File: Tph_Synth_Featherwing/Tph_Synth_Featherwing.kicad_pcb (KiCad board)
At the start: 2 copper layers, 51 x 58.5 mm, 56 parts, among them J1 AudioJack3, J2 Conn_01x04, U1 PAM2401SCADJ, U2 LM2663M, U3 Opamp_Quad_Generic, U4 MCP4728

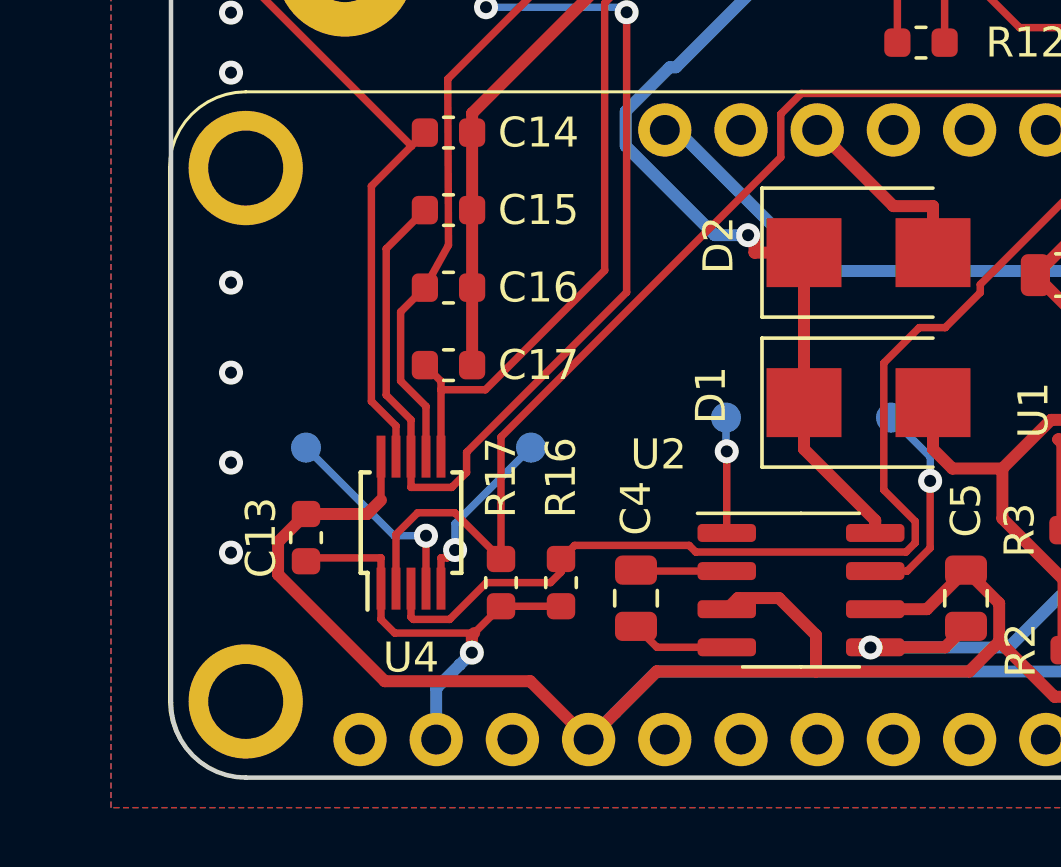
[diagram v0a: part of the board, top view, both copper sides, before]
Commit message: Add Qwiic connector to design
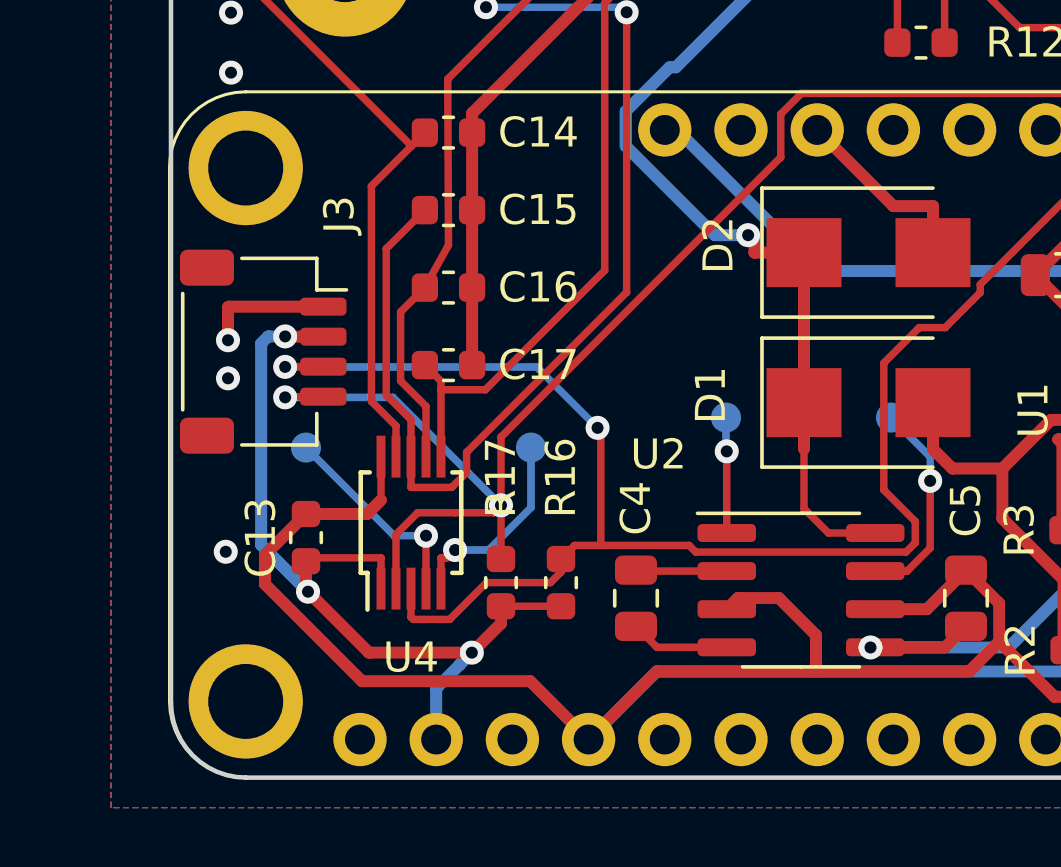
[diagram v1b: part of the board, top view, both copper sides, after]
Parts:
- added J3: Conn_01x04, Connector_JST:JST_SH_SM04B-SRSS-TB_1x04-1MP_P1.00mm_Horizontal, F.Cu at (90.1, 122.3)
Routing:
- net /F_SDA: track 49.7 -> 66.2 mm, vias 0 -> 2
- net +3V3: track 15.2 -> 29.3 mm, vias 1 -> 3
- net /F_SCL: track 48.8 -> 58.3 mm, vias 0 -> 2
- net GND: track 251.4 -> 256.5 mm, vias 33 -> 32
- net +5V: track 46.8 -> 47.8 mm
- net Net-(TP7-Pad1): track 6.06 -> 6.72 mm

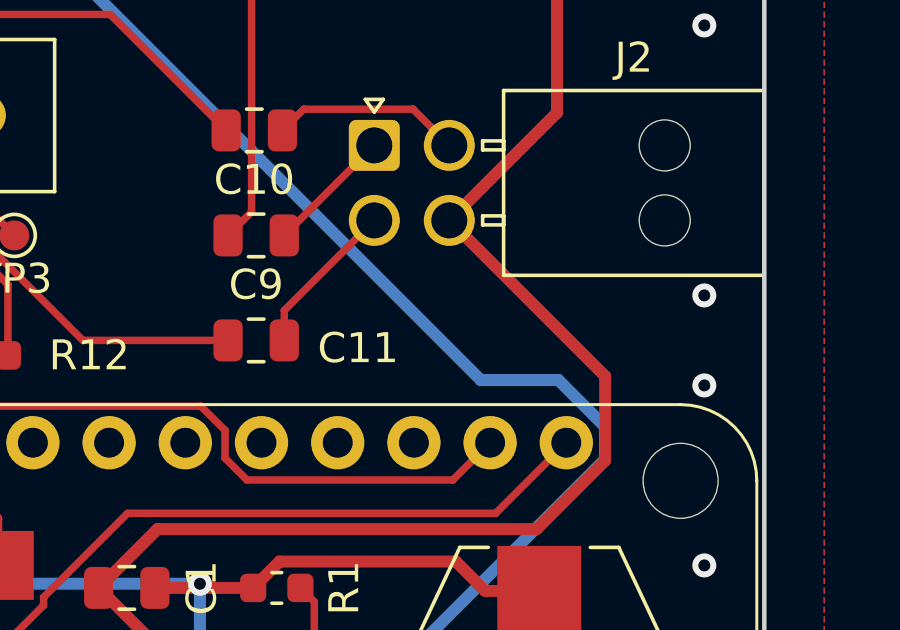
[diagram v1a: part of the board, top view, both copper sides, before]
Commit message: Improve/update silk screen
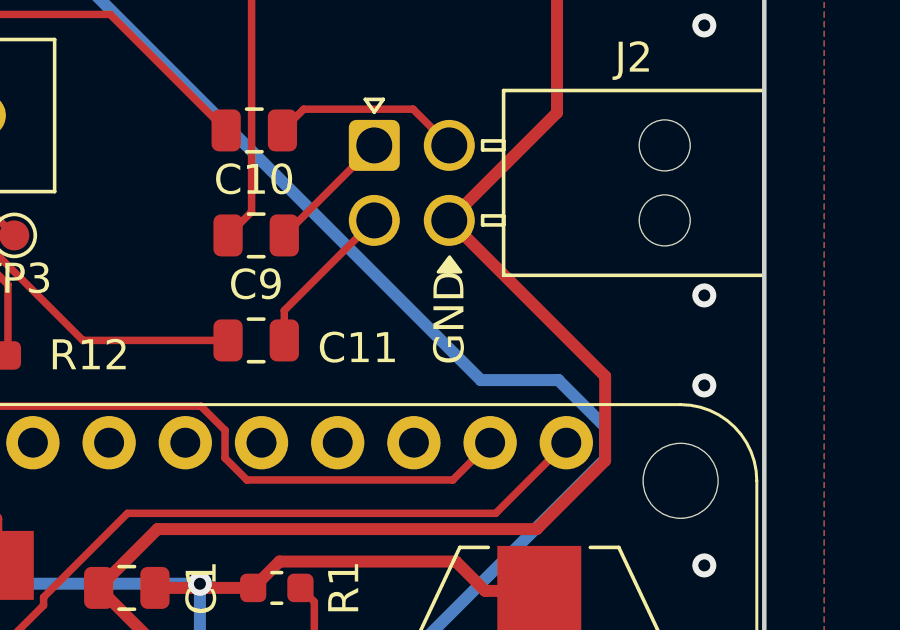
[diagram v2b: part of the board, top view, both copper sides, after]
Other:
- board text added: "3V3"
- board text added: "GND"
- board text added: "SCL"
- board text added: "SDA"
- board text added: "VBAT"
- board text added: "VUSB"
- board text added: "v0.3 20/12/2020 by Tisham (whatnick) Dhar OSHW TAPR"
- board text removed: "v0.2 01/02/2020 by Tisham (whatnick) Dhar OSHW TAPR"
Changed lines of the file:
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@@
       ))
   )
+  (gr_poly (pts
+ (xy 127.889 109.22)
+    (xy 127.127 109.22)
+    (xy 127.508 108.712)) (layer "F.SilkS") (width 0.1))
   (gr_arc (start 135.5 134) (end 135.5 136.5) (angle -90) (layer "Edge.Cuts") (width 0.15))
   (gr_arc (start 135.5 80.5) (end 138 80.5) (angle -90) (layer "Edge.Cuts") (width 0.15))
@@
   (gr_line (start 89.5 78) (end 135.5 78) (layer "Edge.Cuts") (width 0.15))
   (gr_line (start 135.5 136.5) (end 89.5 136.5) (layer "Edge.Cuts") (width 0.15))
+  (gr_text "GND" (at 100.838 132.588 270) (layer "B.SilkS")
+    (effects (font (size 1 1) (thickness 0.15)) (justify mirror))
+  )
+  (gr_text "SCL" (at 128.778 112.141 270) (layer "B.SilkS")
+    (effects (font (size 1 1) (thickness 0.15)) (justify mirror))
+  )
+  (gr_text "SDA" (at 131.445 112.141 270) (layer "B.SilkS")
+    (effects (font (size 1 1) (thickness 0.15)) (justify mirror))
+  )
+  (gr_text "3V3" (at 95.758 132.715 270) (layer "B.SilkS")
+    (effects (font (size 1 1) (thickness 0.15)) (justify mirror))
+  )
+  (gr_text "VUSB" (at 108.458 111.633 270) (layer "B.SilkS")
+    (effects (font (size 1 1) (thickness 0.15)) (justify mirror))
+  )
   (gr_text "3-phase Simulator Featherwing. \nSuitable for use with Teensy Feather\n at around 3.2MHz I2C clock." (at 113.75 98.25) (layer "B.SilkS")
     (effects (font (size 1 1) (thickness 0.25)) (justify mirror))
   )
-  (gr_text "v0.2 01/02/2020\nby Tisham (whatnick) Dhar\nOSHW TAPR" (at 112 120.5) (layer "B.SilkS")
+  (gr_text "v0.3 20/12/2020\nby Tisham (whatnick) Dhar\nOSHW TAPR" (at 112 120.5) (layer "B.SilkS")
     (effects (font (size 1 1) (thickness 0.25)) (justify mirror))
   )
+  (gr_text "VBAT" (at 103.378 111.76 270) (layer "B.SilkS")
+    (effects (font (size 1 1) (thickness 0.15)) (justify mirror))
+  )
+  (gr_text "GND" (at 127.508 110.744 90) (layer "F.SilkS")
+    (effects (font (size 1 1) (thickness 0.15)))
+  )
   (dimension (type aligned) (layer "Dwgs.User")
